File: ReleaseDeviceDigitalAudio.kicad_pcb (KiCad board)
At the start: 4 copper layers, 132 x 68.5 mm, 179 parts, among them J1 Conn_02x08_Counter_Clockwise, J2 ATMEGA_PROG, J3 SignalStrength, J4 UIBoardCON1, J5 Conn_01x04, J6 UIBoardCON2, J7 KeySwitch, Q1 BSS314PEH6327XTSA1, Q3 SQ2362ES-T1_GE3, Q4 SQD50P06-15L_GE3, U1 ATmega4809-A, U10 ULN2003F12FN-7, U11 ULN2003F12FN-7, U12 ULN2003F12FN-7, U13 ULN2003F12FN-7, U14 MAX98089ETN+, U15 SN74LV1T126, U16 SN74LV1T126, U17 BM83SM1-00TA, U18 PCF85063A, U2 VOMA617A, U3 VOMA617A, U4 LM53635LQRNL*Q1, U5 TLVH431AQDBVRQ1, U6 LM74610-Q1, U7 Compute_Module_4_Connectors, U8 CD4514BM, U9 CD4511BPWR, Y1 9HT12

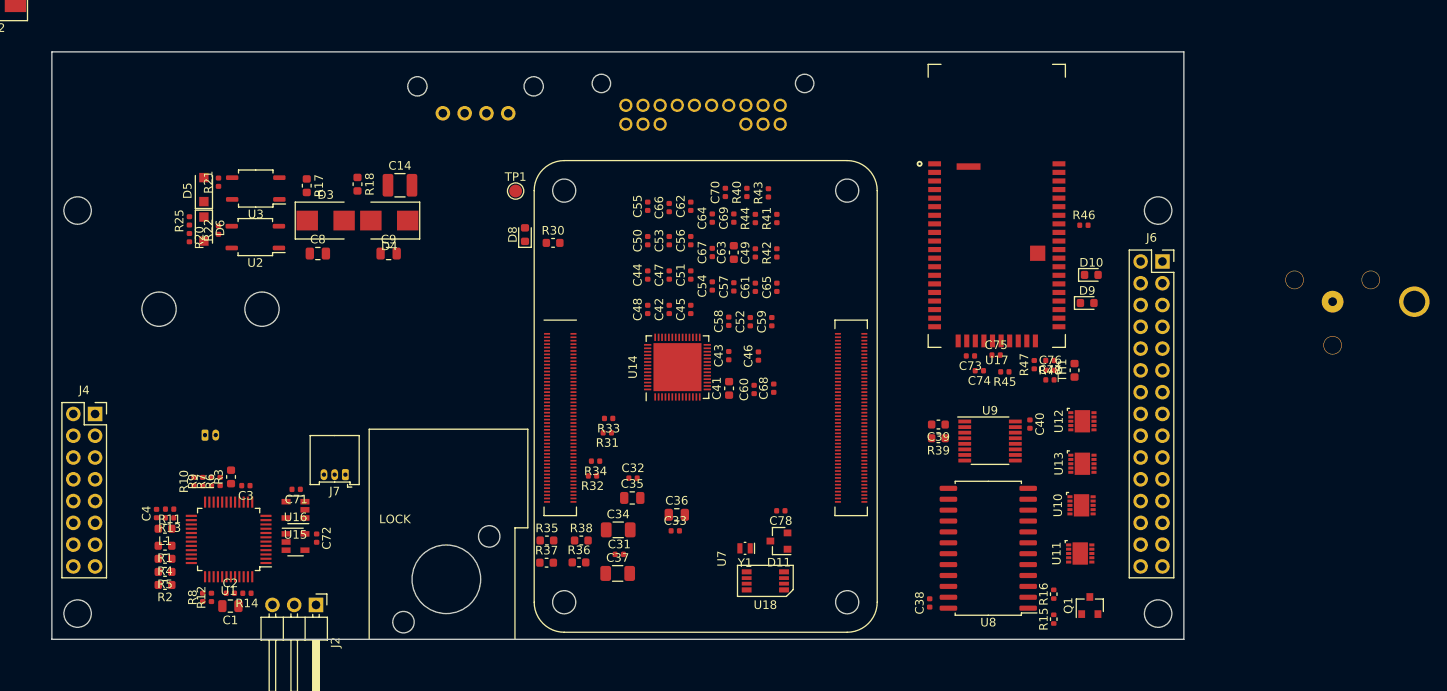
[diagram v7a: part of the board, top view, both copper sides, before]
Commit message: - Ausschnitt für BT Antenne und weitere Optimierungen
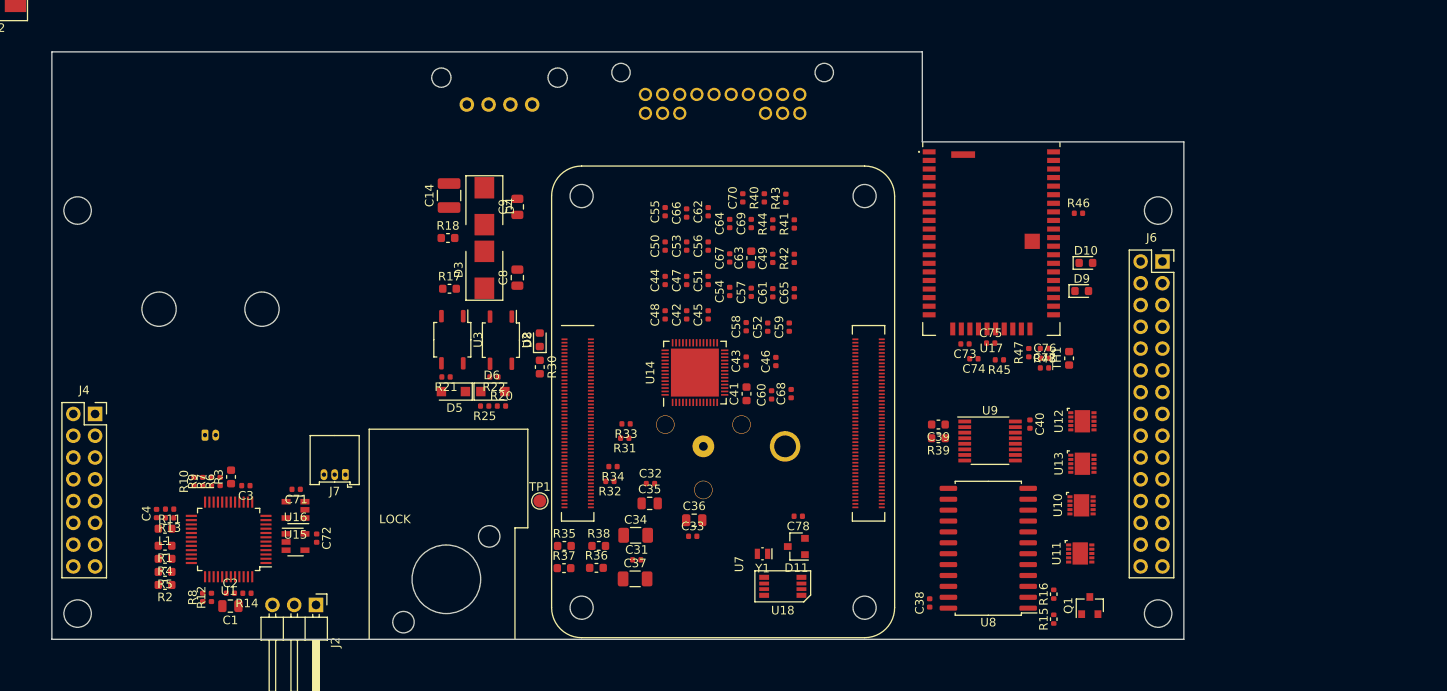
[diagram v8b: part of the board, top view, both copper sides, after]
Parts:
- moved BT1 75.3 mm to (169.5, 107.0)
- moved R20 41.3 mm to (136.4, 102.3), turned to 0 degrees
- moved R25 40.6 mm to (134.5, 102.3), turned to 180 degrees
- moved D6 38.7 mm to (135.4, 100.6), turned to 0 degrees
- moved D5 37.4 mm to (130.8, 100.6), turned to 180 degrees
- moved R22 36.4 mm to (135.5, 98.9), turned to 180 degrees
- moved TP1 36.3 mm to (140.9, 113.4)
- moved R21 34.9 mm to (130.0, 98.9), turned to 180 degrees
- moved U2 31.1 mm to (136.4, 94.6), turned to 270 degrees
- moved U3 28.9 mm to (130.7, 94.6), turned to 270 degrees
- moved C8 23.4 mm to (138.3, 87.3), turned to 90 degrees
- moved R17 20.5 mm to (130.4, 88.6), turned to 0 degrees
- moved D3 19.4 mm to (134.4, 86.4), turned to 90 degrees
- moved C9 16.0 mm to (138.3, 79.1), turned to 90 degrees
- moved R30 14.6 mm to (140.9, 97.8), turned to 270 degrees
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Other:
- outline, holes or cut-outs redrawn
